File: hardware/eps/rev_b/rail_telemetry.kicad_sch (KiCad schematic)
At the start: 27 parts, among them U1300 TMUX1511PWR, U1301 TPS3839K33DBZR

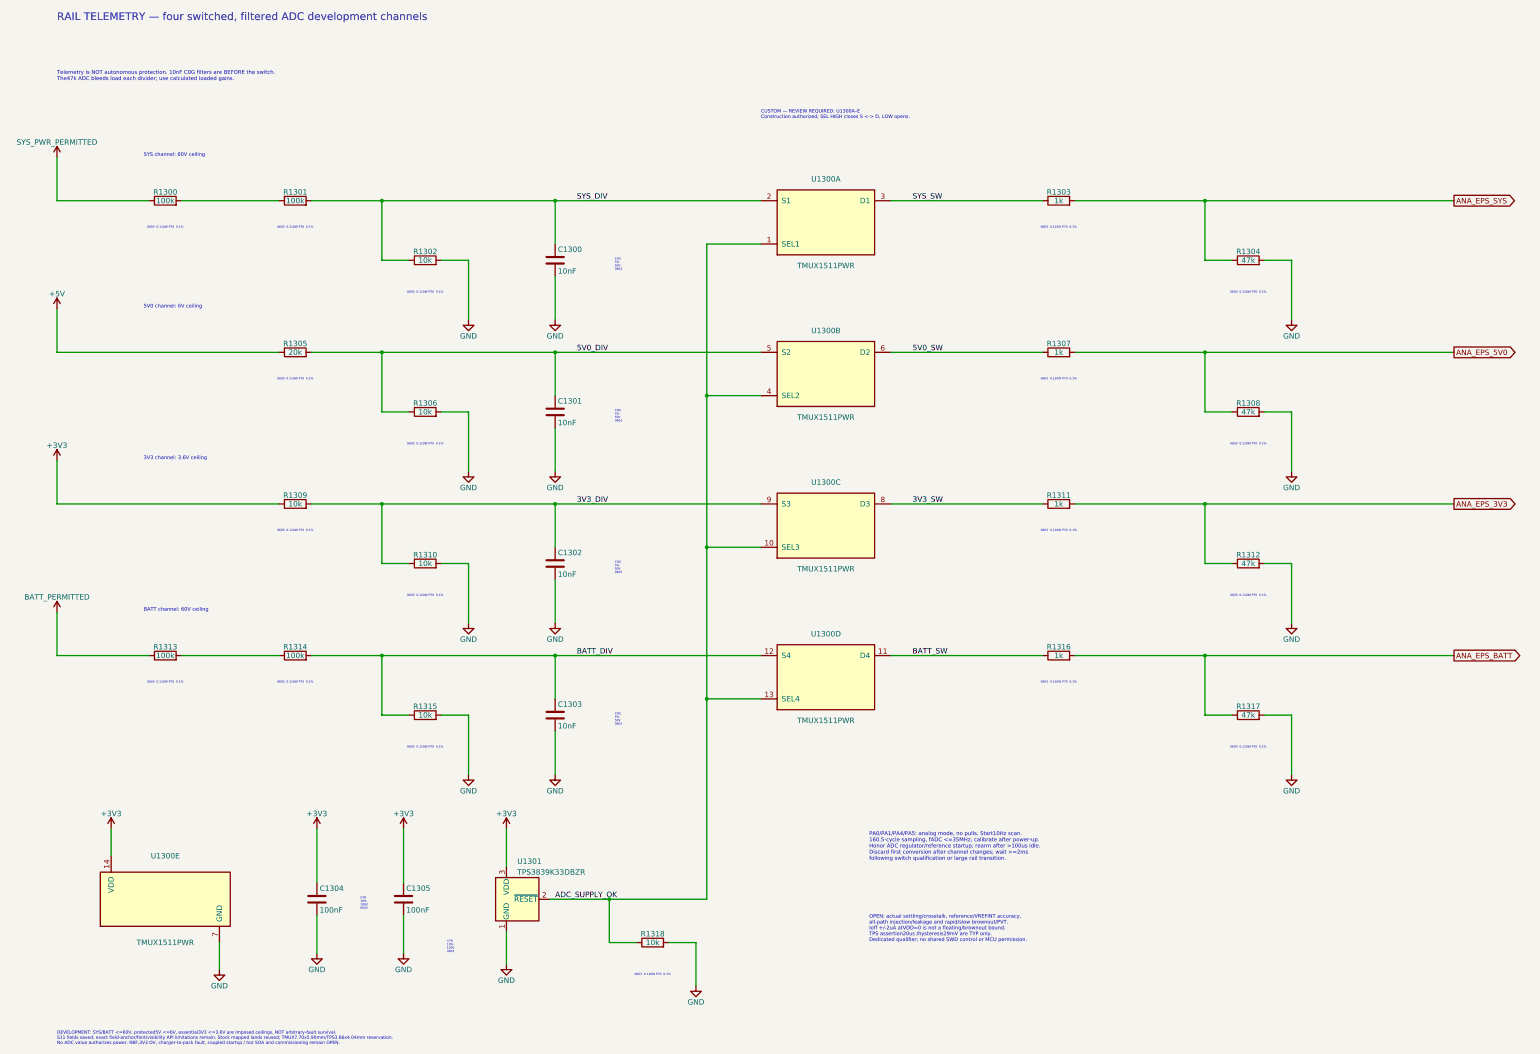
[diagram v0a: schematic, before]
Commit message: Expose native telemetry ratings and verify orientation-aware presentation
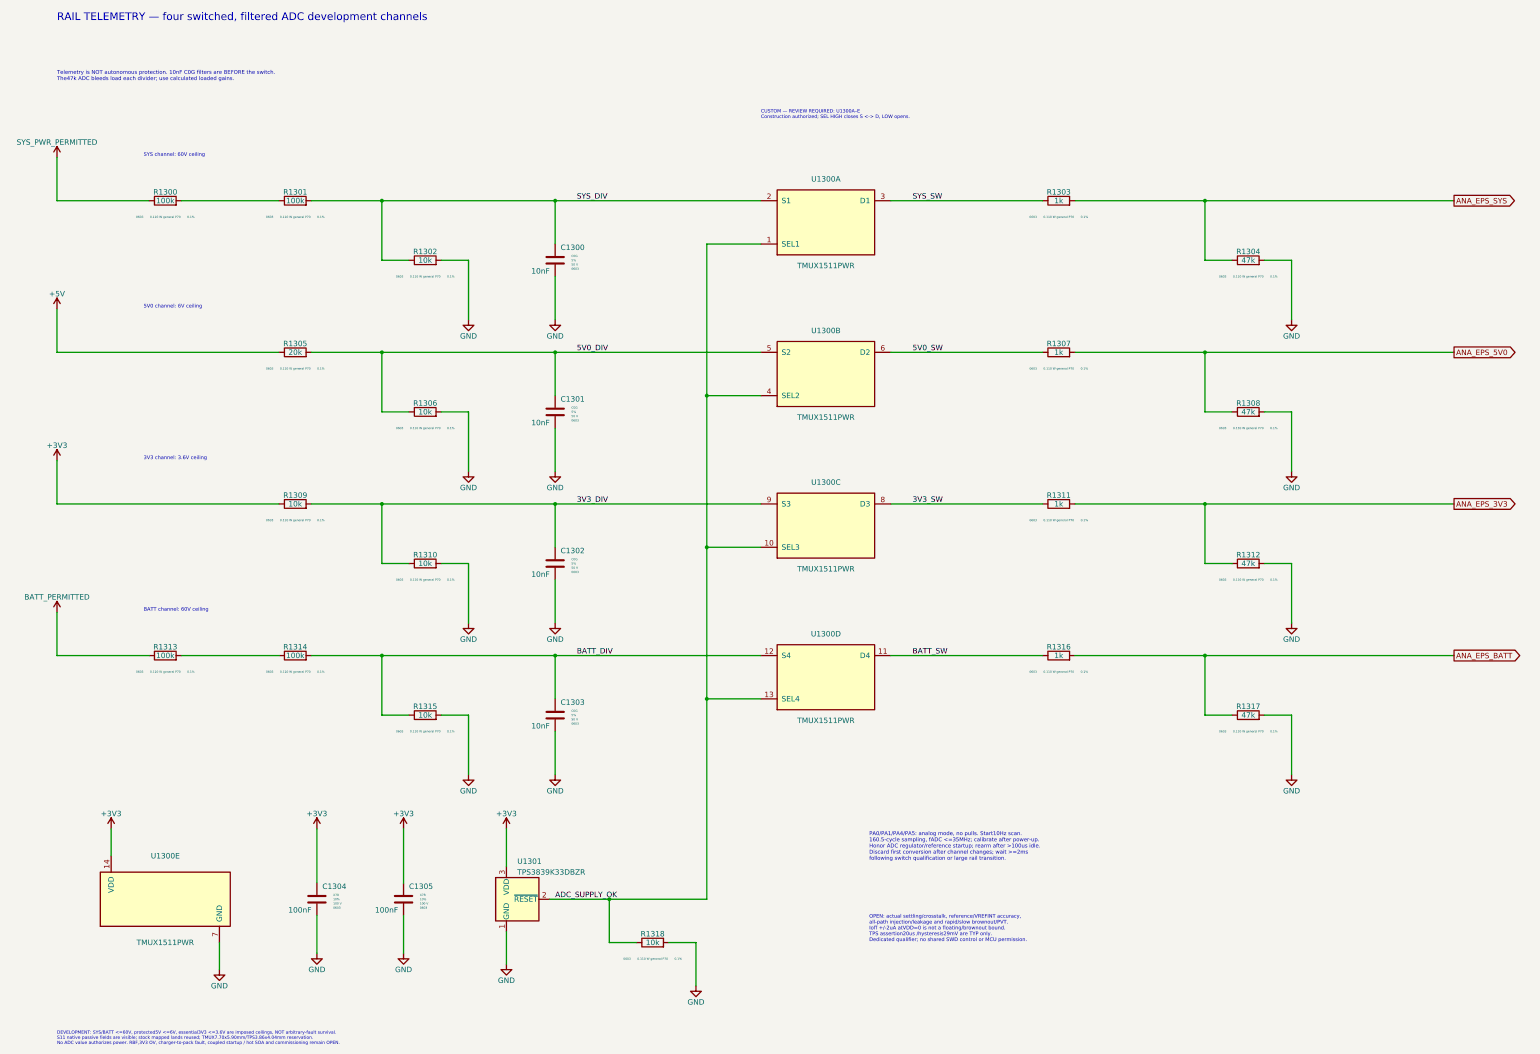
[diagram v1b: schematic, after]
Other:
- note added: "DEVELOPMENT: SYS/BATT <=60V, protected5V <=6V, essential3V3 <=3.6V are imposed ceilings, NOT arbitrary-fault survival. S11 native passive fields are visible; stock mapped lands reused; TMUX7.70x5.90mm/TPS3.86x4.04mm reservation. No ADC value authorizes power. RBF,3V3 OV, charger-to-pack fault, coupled startup / hot SOA and commissioning remain OPEN."
- note removed: "0603 0.110W P70 0.1%"
- note removed: "C0G 5% 50V 0603"
- note removed: "DEVELOPMENT: SYS/BATT <=60V, protected5V <=6V, essential3V3 <=3.6V are imposed ceilings, NOT arbitrary-fault survival. S11 fields saved; exact field-anchor/font/visibility API limitations remain. Stock mapped lands reused; TMUX7.70x5.90mm/TPS3.86x4.04mm reservation. No ADC value authorizes power. RBF,3V3 OV, charger-to-pack fault, coupled startup / hot SOA and commissioning remain OPEN."
- note removed: "X7R 10% 100V 0603"
